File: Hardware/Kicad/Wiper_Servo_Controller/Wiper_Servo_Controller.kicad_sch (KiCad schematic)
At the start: 68 parts, among them J14 12-24V in, J15 Screw_Terminal_01x08, J2 Mot 1 Enc, J3 XLR3, J4 Conn_02x04_Odd_Even, J5 SPI TFT, J6 Conn_02x04_Odd_Even, J7 Mot 2 Enc, J9 UI Inputs, U1 MAX3485, U2 6N137, U3 6N137, U4 6N137, U5 LM1117T-3.3, U6 MCP1700-3302ETO

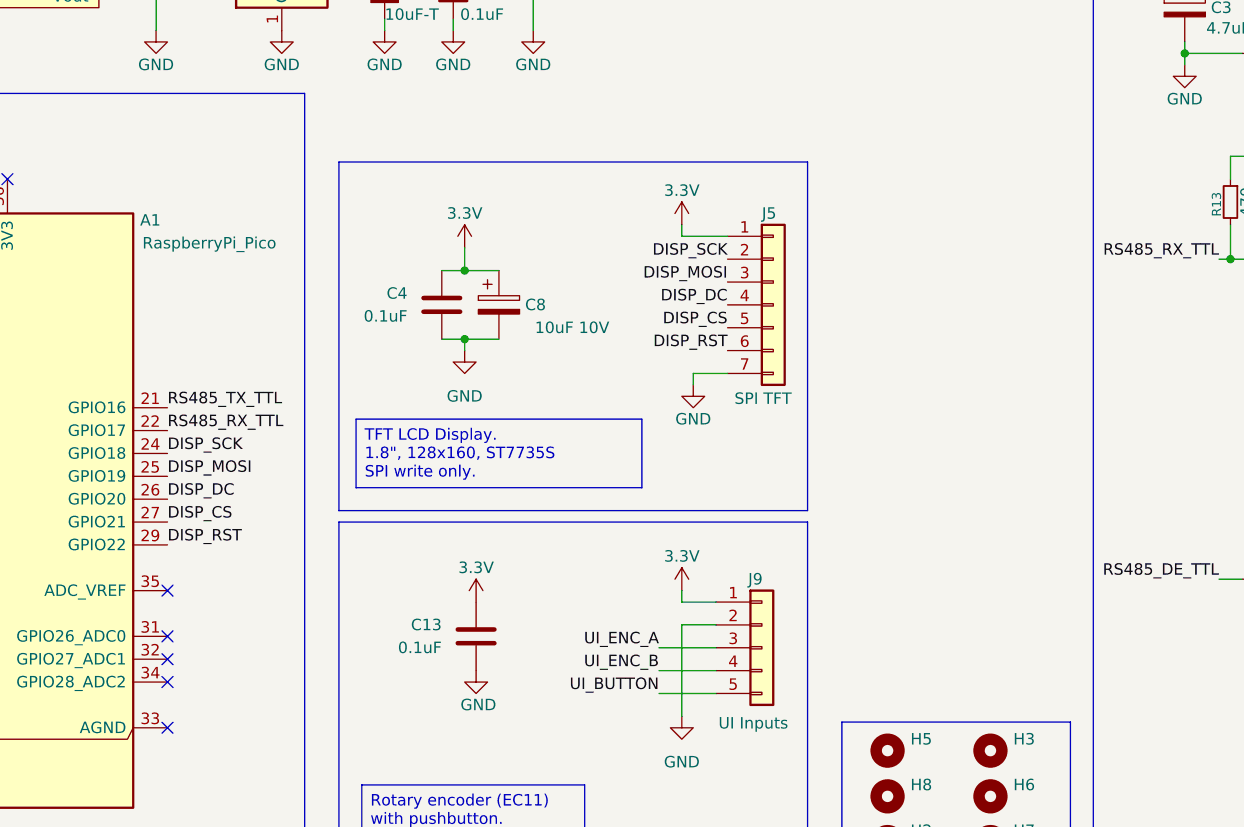
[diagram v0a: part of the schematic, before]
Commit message: Added servo outputs.
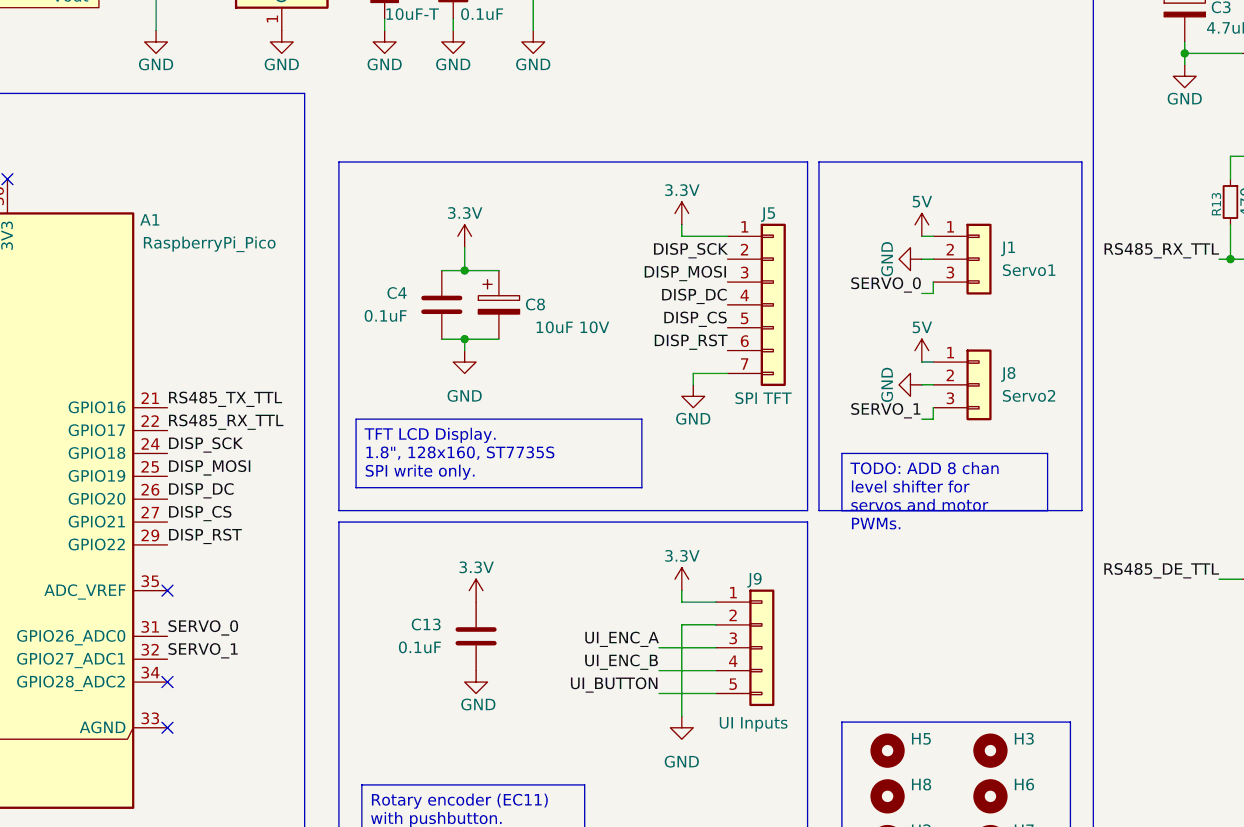
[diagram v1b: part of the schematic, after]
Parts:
- added J1: Servo1, symbol Connector_Generic:Conn_01x03
- added J8: Servo2, symbol Connector_Generic:Conn_01x03
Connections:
- net 5V: now also J1.1 (Pin_1), J8.1 (Pin_1)
- net GND: now also J1.2 (Pin_2), J8.2 (Pin_2)
- net SERVO_0: now reaches A1.31 (GPIO26_ADC0)
- net SERVO_0: now also J1.3 (Pin_3)
- net SERVO_1: now reaches A1.32 (GPIO27_ADC1)
- net SERVO_1: now also J8.3 (Pin_3)
- no-connect marks 22 -> 20

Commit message: Switch from DMX to RS485
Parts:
- removed H3, H4, H6, H7: MountingHole, MountingHole:MountingHole_3.2mm_M3, symbol Mechanical:MountingHole
- removed J3: XLR3, symbol Connector_Audio:XLR3
- added C11: 10uF-T, Capacitor_THT:CP_Radial_Tantal_D5.5mm_P2.50mm, symbol Device:C_Polarized_Small
- added C13: 4.7uF, Capacitor_THT:CP_Radial_D5.0mm_P2.00mm, symbol Device:C_Polarized
- added J11: RS485, Connector_JST:JST_PH_B3B-PH-K_1x03_P2.00mm_Vertical, symbol Connector_Generic:Conn_01x03
- J10: renamed from J8; footprint (none) -> Connector_JST:JST_PH_B3B-PH-K_1x03_P2.00mm_Vertical
- J6: renamed from J9; footprint (none) -> Connector_JST:JST_PH_B5B-PH-K_1x05_P2.00mm_Vertical
- J7: renamed from J5; footprint (none) -> Connector_JST:JST_PH_B7B-PH-K_1x07_P2.00mm_Vertical
- J9: renamed from J1; footprint (none) -> Connector_JST:JST_PH_B3B-PH-K_1x03_P2.00mm_Vertical
- JP1: footprint (none) -> Jumper:SolderJumper-2_P1.3mm_Open_Pad1.0x1.5mm
- TP1: renamed from TP6; footprint TestPoint:TestPoint_Loop_D2.50mm_Drill1.0mm -> TestPoint:TestPoint_THTPad_D1.5mm_Drill0.7mm
- TP2: renamed from TP7; footprint TestPoint:TestPoint_Loop_D2.50mm_Drill1.0mm -> TestPoint:TestPoint_THTPad_D1.5mm_Drill0.7mm
- TP3: renamed from TP8; footprint TestPoint:TestPoint_Loop_D2.50mm_Drill1.0mm -> TestPoint:TestPoint_THTPad_D1.5mm_Drill0.7mm
- TP4: renamed from TP3; footprint TestPoint:TestPoint_Loop_D2.50mm_Drill1.0mm -> TestPoint:TestPoint_THTPad_D1.5mm_Drill0.7mm
- TP5: footprint TestPoint:TestPoint_Loop_D2.50mm_Drill1.0mm -> TestPoint:TestPoint_THTPad_D1.5mm_Drill0.7mm
- TP6: renamed from TP1; value DMX_RX -> ~; footprint TestPoint:TestPoint_Loop_D2.50mm_Drill1.0mm -> TestPoint:TestPoint_THTPad_D1.5mm_Drill0.7mm
- U1: renamed from U8; value ~ -> DCDC 5V
- U3: renamed from U2; footprint Package_DIP:DIP-8_W7.62mm -> Package_DIP:SMDIP-8_W9.53mm
- U4: renamed from U3; footprint Package_DIP:DIP-8_W7.62mm -> Package_DIP:SMDIP-8_W9.53mm
- U5: renamed from U4; footprint Package_DIP:DIP-8_W7.62mm -> Package_DIP:SMDIP-8_W9.53mm
- renumbered C2 to C1, C8 to C10, C3 to C12, C9 to C18, C11 to C19, C1 to C2, C6 to C3, C10 to C4, C12 to C5, C5 to C6, C4 to C7, C7 to C8, C13 to C9, H5 to H1, H8 to H2, H2 to H3, H1 to H4, J14 to J1, J4 to J2, J6 to J3, J2 to J4, J7 to J5, J15 to J8, R16 to R10, R17 to R11, R14 to R12, R15 to R13, R12 to R14, R9 to R15, R11 to R16, R10 to R17, R4 to R2, R2 to R3, R5 to R4, R3 to R5, R7 to R6, R8 to R7, R6 to R8, R13 to R9, U5 to U2, U1 to U6, U6 to U7
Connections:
- net +5V_ISO: now also C13.1
- net 5V: now also C11.1
- net GND: now also C11.2
- net GND_ISO: now also C13.2
- net MOT_1_ESTOP_A: now also J8.1 (Pin_1); no longer J8.7 (Pin_7)
- net MOT_1_ESTOP_B: now also J8.3 (Pin_3); no longer J8.5 (Pin_5)
- net MOT_2_ESTOP_A: now also J8.5 (Pin_5); no longer J8.3 (Pin_3)
- net MOT_2_ESTOP_B: now also J8.7 (Pin_7); no longer J8.1 (Pin_1)
- net RS485_A: now also J11.1 (Pin_1)
- net RS485_B: now also J11.2 (Pin_2)
- net at JP1.2 (B): now also J11.3 (Pin_3)
- net RS485_VCC renamed +3.3V_ISO
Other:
- added sheet Cable_Diagrams (cable_diagrams.kicad_sch)
- moved on the sheet: C12, C14, C15, C16, C17, C18, C19, J10, J8, J9, JP1, PS1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
